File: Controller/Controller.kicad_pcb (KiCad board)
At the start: 2 copper layers, 99.1 x 81.3 mm, 74 parts, among them J1 Prog, J2 NTC Conn, J3 PWR, J4 Heater, J5 Pololu reg16a 3V3, Q1 BC547, Q2 BC547, Q3 IRF5305, SW3 Reset, SW4 Flash, U1 ESP-12E, U2 MCP3208, U3 LM324, U4 LM393, U5 LM78L05_TO92

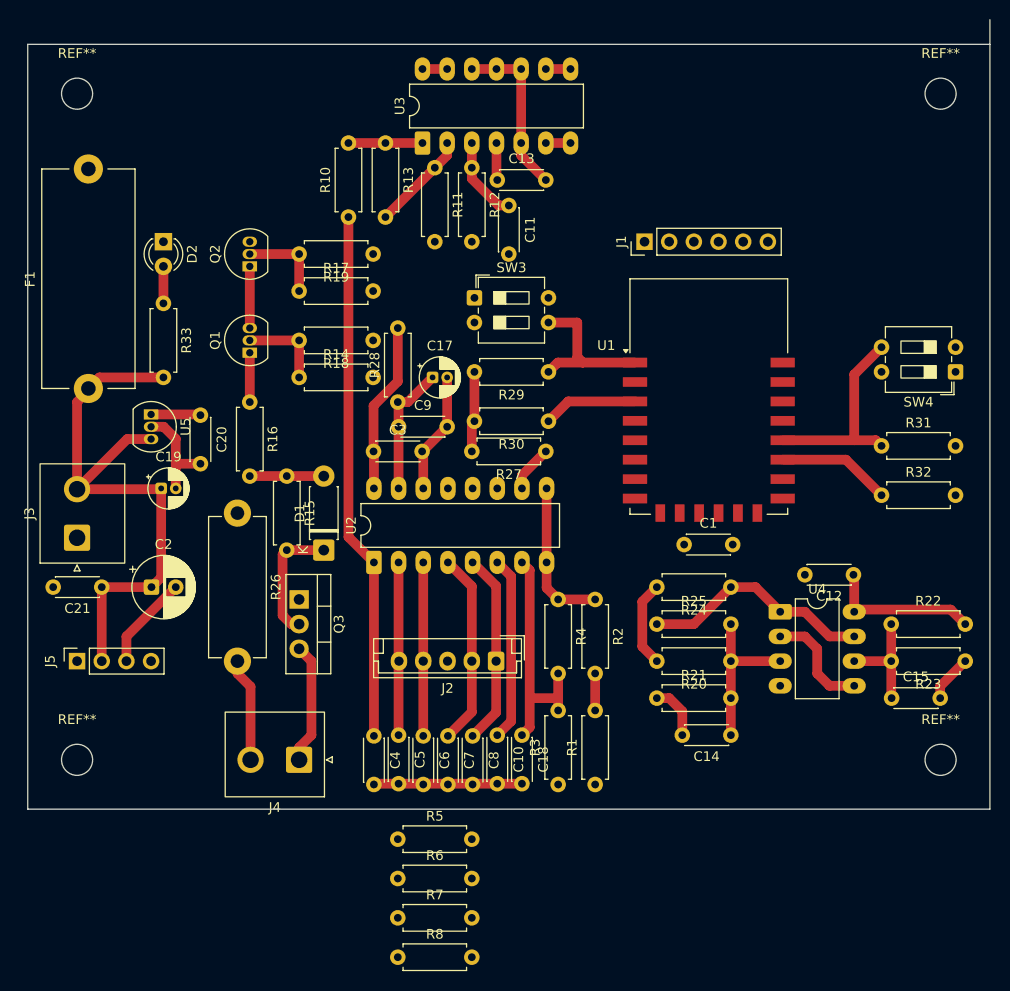
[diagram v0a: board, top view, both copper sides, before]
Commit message: Switch to Teensy Pro Micro
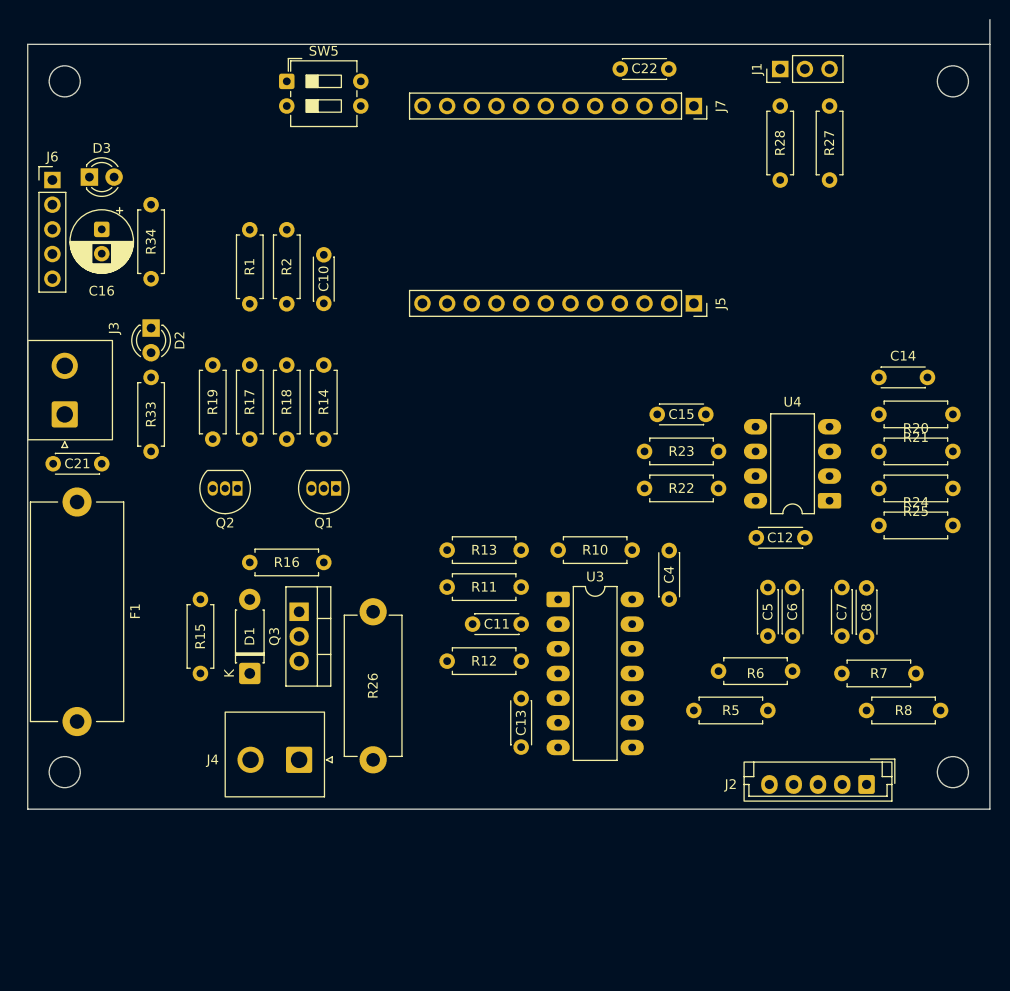
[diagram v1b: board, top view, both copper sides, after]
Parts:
- removed C1, C18, C20, C3, C9: 100n, Capacitor_THT:C_Disc_D4.3mm_W1.9mm_P5.00mm
- removed C17, C19: 4u7, Capacitor_THT:CP_Radial_D4.0mm_P1.50mm
- removed C2: 47u, Capacitor_THT:CP_Radial_D6.3mm_P2.50mm
- removed R29, R30, R31, R32: 10k, Resistor_THT:R_Axial_DIN0207_L6.3mm_D2.5mm_P7.62mm_Horizontal
- removed R3: 15k, Resistor_THT:R_Axial_DIN0207_L6.3mm_D2.5mm_P7.62mm_Horizontal
- removed R4: 22k, Resistor_THT:R_Axial_DIN0207_L6.3mm_D2.5mm_P7.62mm_Horizontal
- removed the REF** at (132.1, 73.7)
- removed the REF** at (221.0, 73.7)
- removed the REF** at (132.1, 142.2)
- removed the REF** at (221.0, 142.2)
- removed SW3: Reset, Button_Switch_THT:SW_DIP_SPSTx02_Slide_6.7x6.64mm_W7.62mm_P2.54mm_LowProfile
- removed SW4: Flash, Button_Switch_THT:SW_DIP_SPSTx02_Slide_6.7x6.64mm_W7.62mm_P2.54mm_LowProfile
- removed U1: ESP-12E, RF_Module:ESP-12E
- removed U2: MCP3208, Package_DIP:DIP-16_W7.62mm_LongPads
- removed U5: LM78L05_TO92, Package_TO_SOT_THT:TO-92_Inline
- added C16: 47u, Capacitor_THT:CP_Radial_D6.3mm_P2.50mm, F.Cu at (134.6, 87.6)
- added C22: 100n, Capacitor_THT:C_Disc_D4.3mm_W1.9mm_P5.00mm, F.Cu at (188.0, 71.1)
- added D3: gn, LED_THT:LED_D3.0mm, F.Cu at (133.3, 82.2)
- added J6: Pololu reg17a 5V, Connector_PinHeader_2.54mm:PinHeader_1x05_P2.54mm_Vertical, F.Cu at (129.5, 82.5)
- added J7: PM2, Connector_PinSocket_2.54mm:PinSocket_1x12_P2.54mm_Vertical, F.Cu at (195.6, 74.9)
- added R34: 4k7, Resistor_THT:R_Axial_DIN0207_L6.3mm_D2.5mm_P7.62mm_Horizontal, F.Cu at (139.7, 85.1)
- added REF**: MountingHole_3.2mm_M3_DIN965, MountingHole:MountingHole_3.2mm_M3_DIN965, F.Cu at (222.2, 143.5)
- added REF**: MountingHole_3.2mm_M3_DIN965, MountingHole:MountingHole_3.2mm_M3_DIN965, F.Cu at (130.8, 143.5)
- added REF**: MountingHole_3.2mm_M3_DIN965, MountingHole:MountingHole_3.2mm_M3_DIN965, F.Cu at (222.2, 72.4)
- added REF**: MountingHole_3.2mm_M3_DIN965, MountingHole:MountingHole_3.2mm_M3_DIN965, F.Cu at (130.8, 72.4)
- added SW5: Reset, Button_Switch_THT:SW_DIP_SPSTx02_Slide_6.7x6.64mm_W7.62mm_P2.54mm_LowProfile, F.Cu at (153.7, 72.4)
- J1: value Prog -> UART; footprint Connector_PinHeader_2.54mm:PinHeader_1x06_P2.54mm_Vertical -> Connector_PinHeader_2.54mm:PinHeader_1x03_P2.54mm_Vertical
- J5: value Pololu reg16a 3V3 -> PM1; footprint Connector_PinSocket_2.54mm:PinSocket_1x04_P2.54mm_Vertical -> Connector_PinSocket_2.54mm:PinSocket_1x12_P2.54mm_Vertical
- R1: value 100k -> 68k
- R13: value 56k -> 68k
- R27: value 10k -> 1k
- R28: value 10R -> 1k
- R33: value 470R -> 10k
- moved J5 73.4 mm to (195.6, 95.2), turned to -90 degrees
- moved R1 67.3 mm to (149.9, 87.7), turned to -90 degrees
- moved R8 61.4 mm to (221.0, 137.2), turned to 180 degrees
- moved R7 59.0 mm to (218.4, 133.3), turned to 180 degrees
- moved C13 53.4 mm to (177.8, 135.9), turned to -90 degrees
- moved R12 51.1 mm to (177.8, 132.1), turned to 180 degrees
- moved R2 49.6 mm to (153.7, 87.7)
- moved U3 49.0 mm to (181.6, 125.7), turned to 0 degrees
- moved C10 47.9 mm to (157.5, 95.2), turned to 90 degrees
- moved R28 45.5 mm to (204.5, 82.5)
- moved R10 45.0 mm to (189.2, 120.7), turned to 180 degrees
- moved R13 44.2 mm to (177.8, 120.7), turned to 180 degrees
- moved R11 44.1 mm to (177.8, 124.5), turned to 180 degrees
- moved C11 43.1 mm to (177.8, 128.3), turned to 180 degrees
- moved R21 42.2 mm to (222.2, 106.7), turned to 180 degrees
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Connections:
- C12 pad 1: +3V3 -> +24V
- J1 pad 1: +3V3 -> Net-(J1-Pin_1)
- J1 pad 2: /FLASH -> GND
- J1 pad 3: /RESET -> Net-(J1-Pin_3)
- J2 pad 3: +3V3 -> +5V
- J3 pad 1: GND -> +24V
- J3 pad 2: +24V -> GND
- J4 pad 1: HEATER_POS -> HEATER_NEG
- J4 pad 2: HEATER_NEG -> HEATER_POS
- J5 pad 1: unconnected-(J5-Pin_1-Pad1) -> UART_TX
- J5 pad 2: +24V -> UART_RX
- J5 pad 4: +3V3 -> GND
- R20 pad 2: +3V3 -> +5V
- R22 pad 2: +3V3 -> +5V
- R24 pad 2: +3V3 -> +5V
- R27 pad 1: MCP3208 CS -> UART_TX
- R27 pad 2: +3V3 -> Net-(J1-Pin_3)
- R28 pad 1: Net-(U2-Vref) -> UART_RX
- R28 pad 2: +3V3 -> Net-(J1-Pin_1)
- U4 pad 2: ADC_NTC_T5 -> ADC_NTC_SAFE
- U4 pad 5: ADC_NTC_T5 -> ADC_NTC_SAFE
- U4 pad 8: +3V3 -> +24V
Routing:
- net GND: track 92.1 -> 0.00 mm
- net +24V: track 60.8 -> 0.00 mm
- net ADC_HEATER_CURRENT: track 54.5 -> 0.00 mm
- net +3V3: track 50.7 -> 0.00 mm
- net ADC_5V: track 25.2 -> 0.00 mm
- net SAFETY_OK: track 24.0 -> 0.00 mm
- net ADC_24V: track 22.8 -> 0.00 mm
- net /FLASH: track 21.2 -> 0.00 mm
- net ADC_NTC_T3: track 19.9 -> 0.00 mm
- net ADC_NTC_SAFE: track 19.9 -> 0.00 mm
- net ADC_NTC_T2: track 17.9 -> 0.00 mm
- net ADC_NTC_T1: track 17.8 -> 0.00 mm
- net /RESET: track 16.6 -> 0.00 mm
- net Net-(U4A-+): track 16.5 -> 0.00 mm
- net Net-(U2-Vref): track 13.6 -> 0.00 mm
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
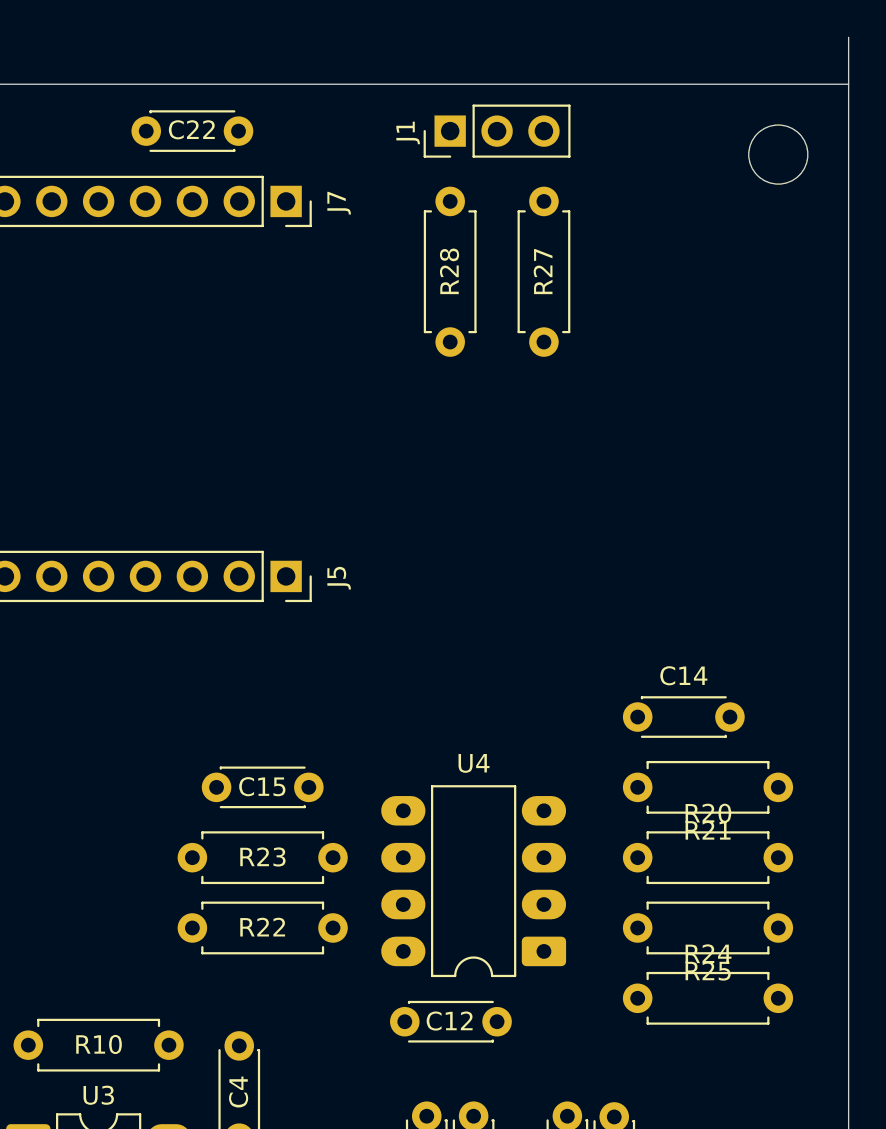
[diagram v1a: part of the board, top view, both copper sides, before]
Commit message: Suppress backfeeding from Vbus to +5V rail
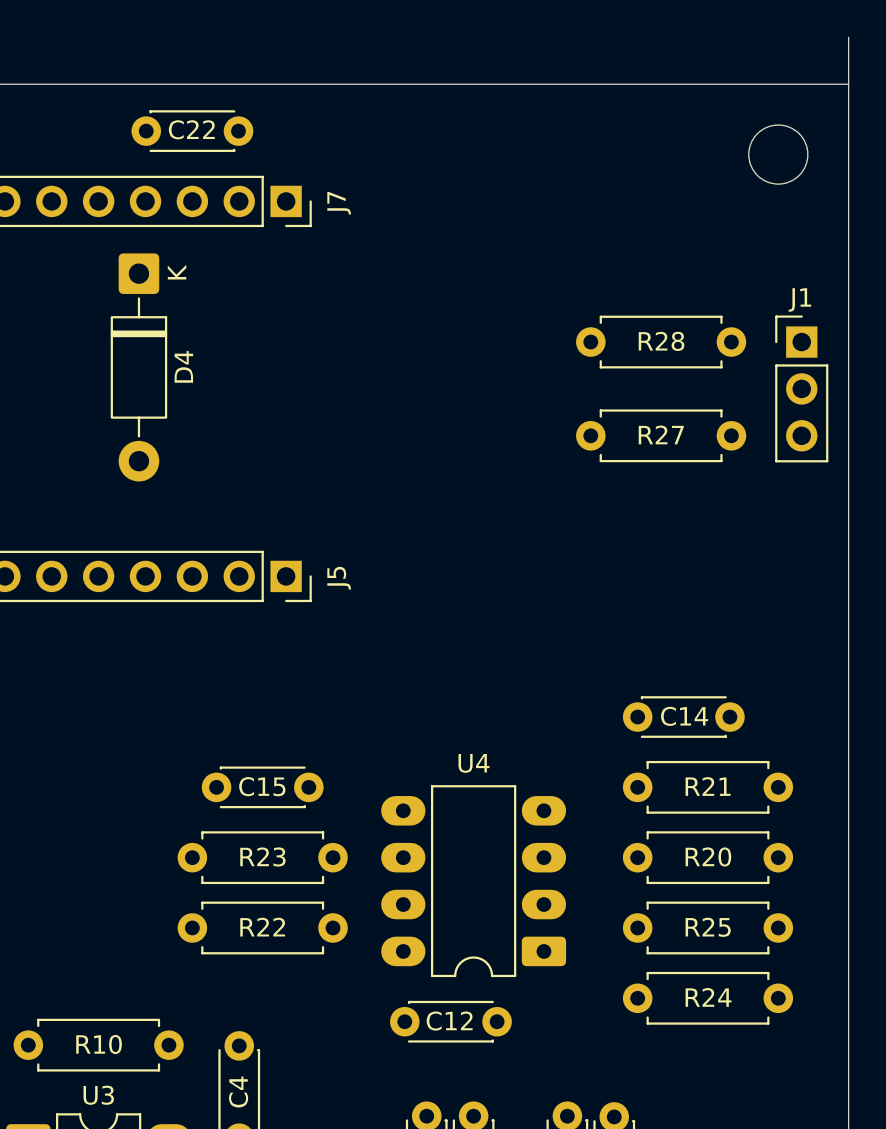
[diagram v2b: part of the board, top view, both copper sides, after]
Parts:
- added D4: 1N5817, Diode_THT:D_DO-41_SOD81_P10.16mm_Horizontal, F.Cu at (187.6, 78.8)
- R22: value 56k -> 68k
- moved J1 22.2 mm to (223.5, 82.5), turned to 0 degrees
- moved R28 7.62 mm to (212.1, 82.5), turned to 0 degrees
- moved R27 5.68 mm to (212.1, 87.6), turned to 0 degrees
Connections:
- C22 pad 1: +5V -> Net-(D4-K)
- J7 pad 4: +5V -> Net-(D4-K)
